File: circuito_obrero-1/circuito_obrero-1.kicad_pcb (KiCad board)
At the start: 2 copper layers, 112 x 49 mm, 30 parts, among them U1 74HC165, U2 74HC165

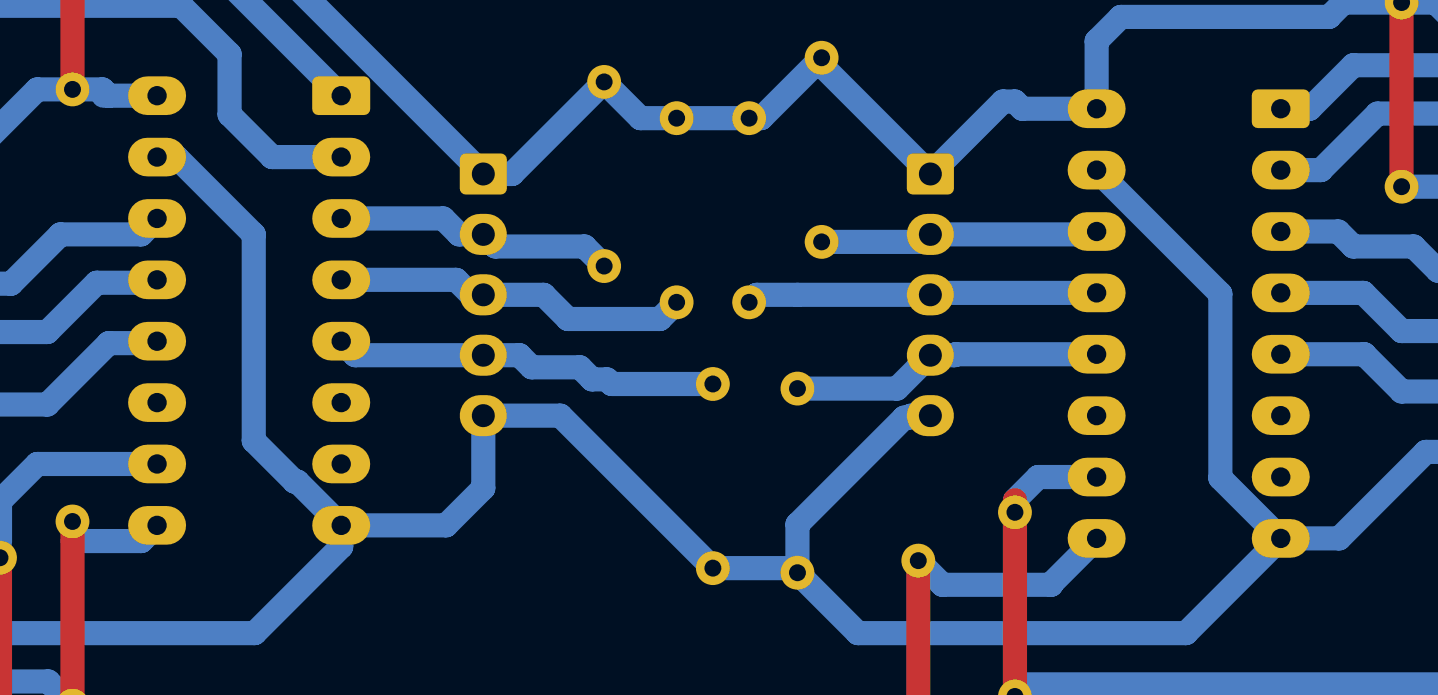
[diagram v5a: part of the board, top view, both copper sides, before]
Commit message: pines sueltos a gnd
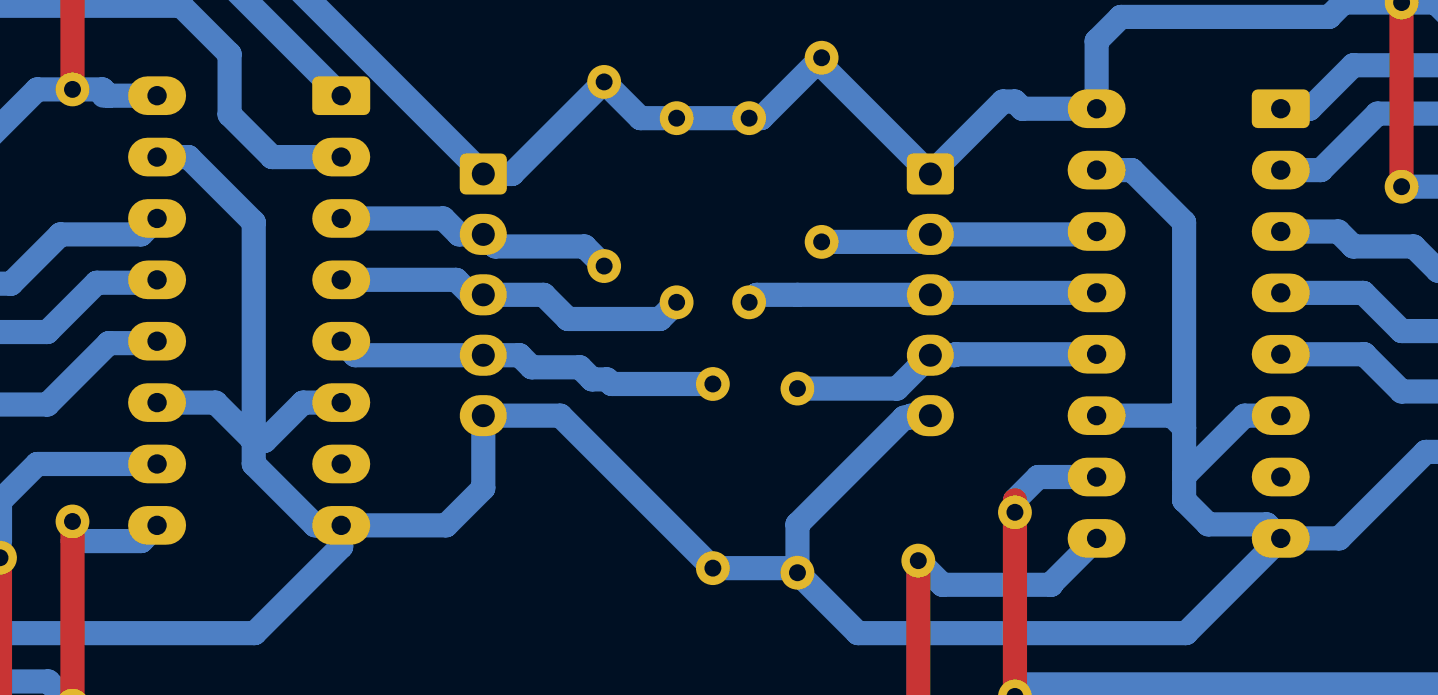
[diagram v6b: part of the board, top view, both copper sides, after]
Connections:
- U1 pad 11: unconnected-(U1-D0-Pad11) -> GND
- U1 pad 6: unconnected-(U1-D7-Pad6) -> GND
- U2 pad 11: unconnected-(U2-D0-Pad11) -> GND
- U2 pad 6: unconnected-(U2-D7-Pad6) -> GND
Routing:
- net GND: track 173.0 -> 193.9 mm
